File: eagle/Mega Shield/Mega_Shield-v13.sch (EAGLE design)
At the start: 27 parts, among them U1 LCD-16X2SILK, U2 LCD-16X2SILK, U3 MAX232PTH

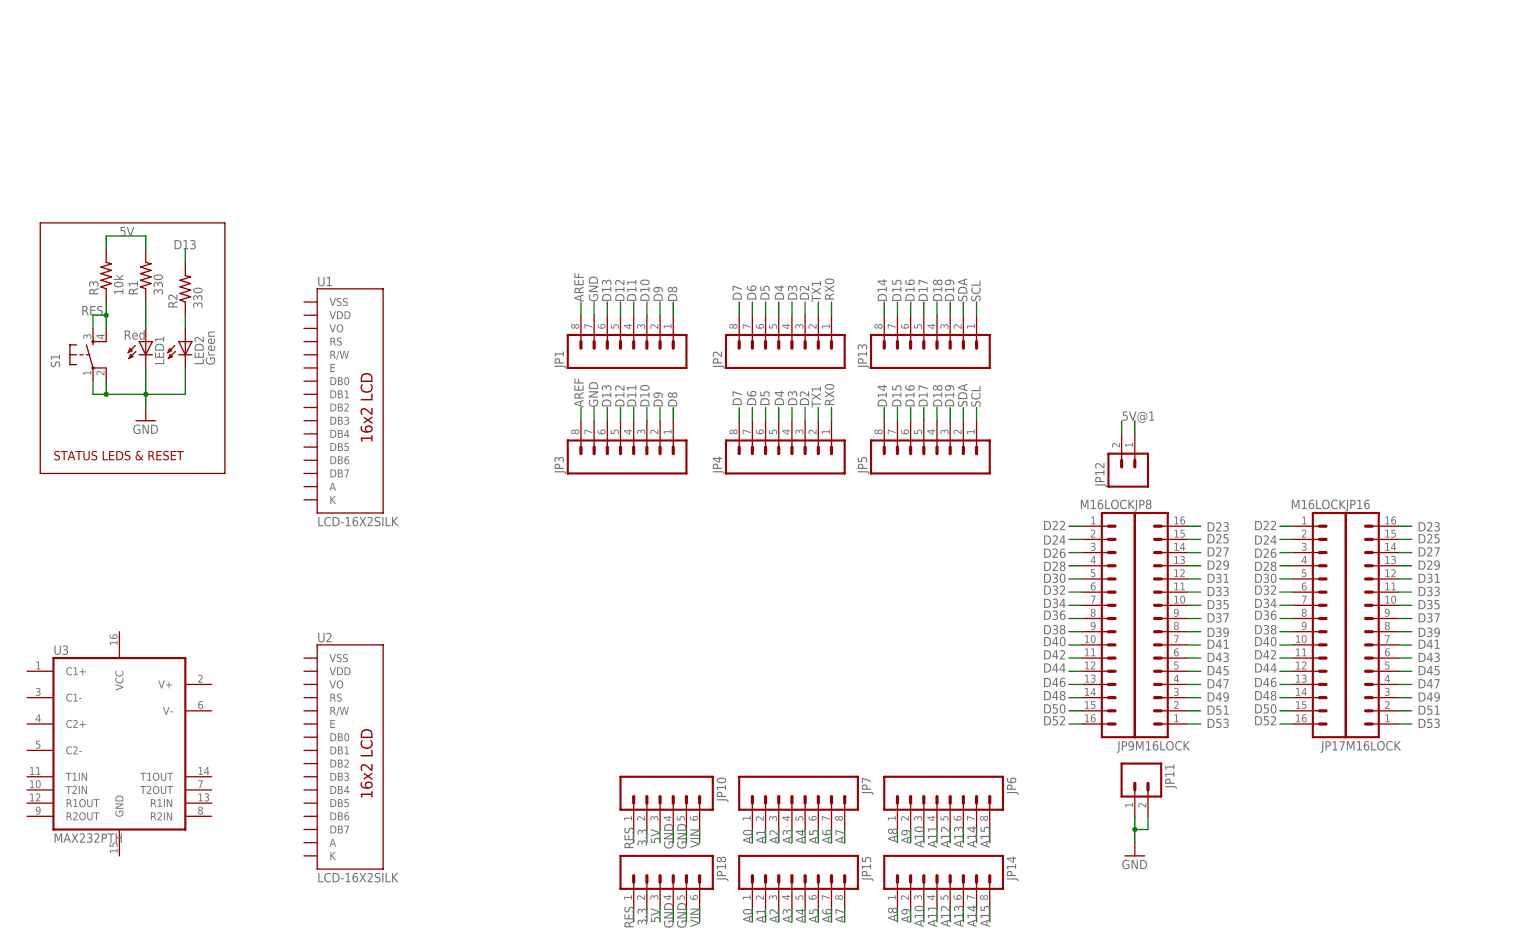
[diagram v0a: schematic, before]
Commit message: working on pcb, added main connector and lcds
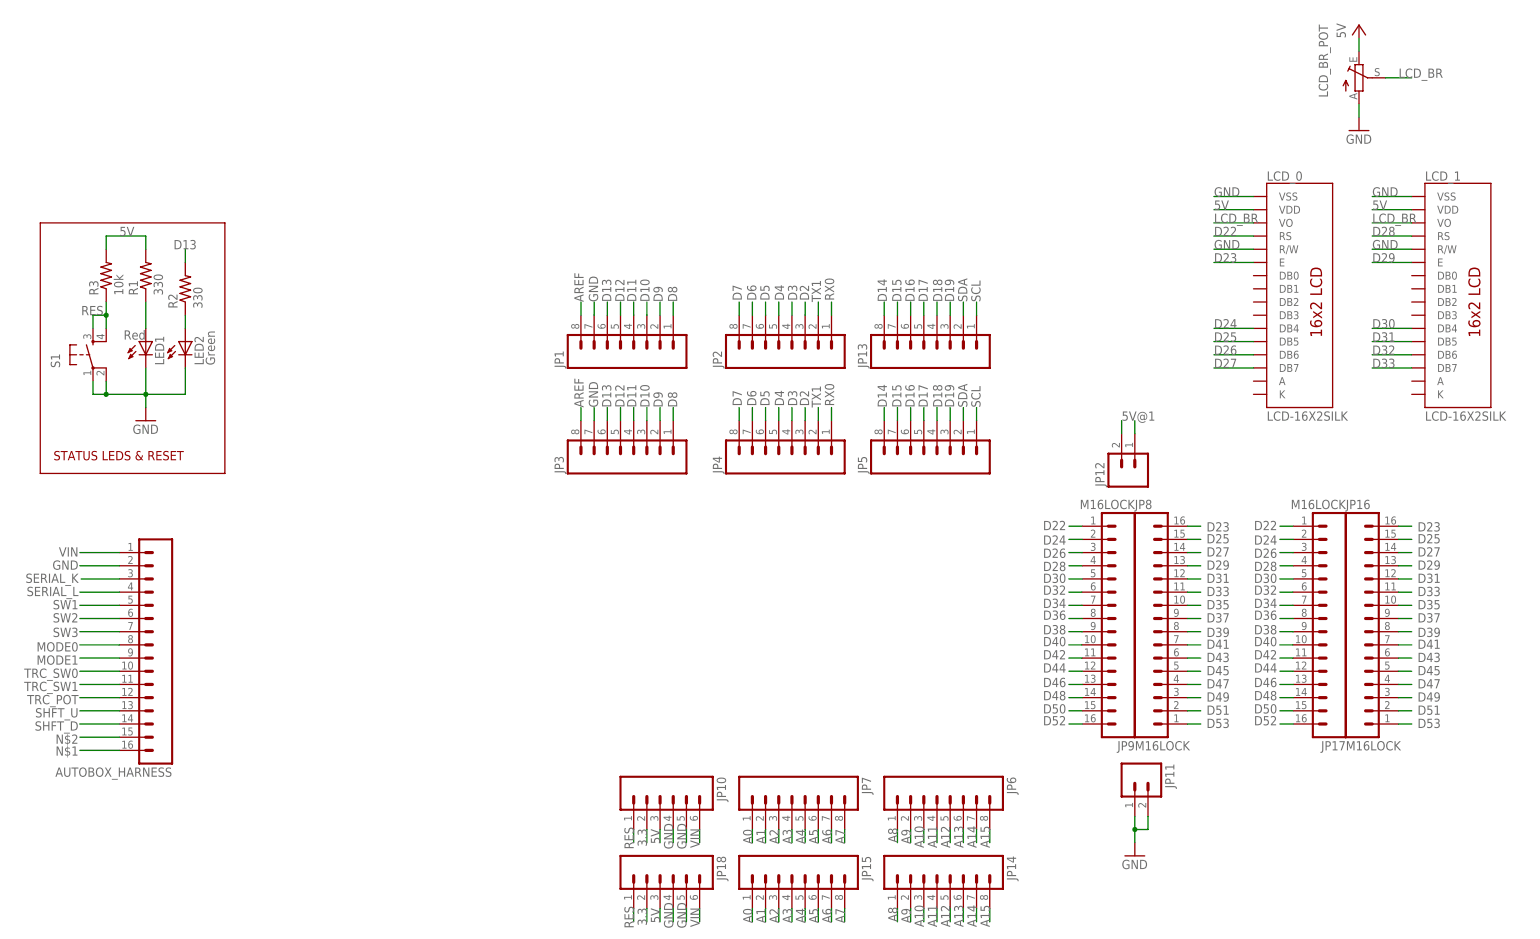
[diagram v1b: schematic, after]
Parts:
- removed U1, U2: LCD-16X2SILK, SparkFun-Displays:LCD-16X2SILK
- removed U3: MAX232PTH, SparkFun-DigitalIC:MAX232PTH
- added AUTOBOX_HARNESS: (no value), con-amp-quick:M16
- added LCD_0, LCD_1: LCD-16X2SILK, SparkFun-Displays:LCD-16X2SILK
- added LCD_BR_POT: (no value), pot:TRIM_EU-CA14V
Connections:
- new net LCD_BR: LCD_0.VO, LCD_1.VO, LCD_BR_POT.S
- new net MODE0: AUTOBOX_HARNESS.8
- new net MODE1: AUTOBOX_HARNESS.9
- new net N$1: AUTOBOX_HARNESS.16
- new net N$2: AUTOBOX_HARNESS.15
- new net SERIAL_K: AUTOBOX_HARNESS.3
- new net SERIAL_L: AUTOBOX_HARNESS.4
- new net SHFT_D: AUTOBOX_HARNESS.14
- new net SHFT_U: AUTOBOX_HARNESS.13
- new net SW1: AUTOBOX_HARNESS.5
- new net SW2: AUTOBOX_HARNESS.6
- new net SW3: AUTOBOX_HARNESS.7
- new net TRC_POT: AUTOBOX_HARNESS.12
- new net TRC_SW0: AUTOBOX_HARNESS.10
- new net TRC_SW1: AUTOBOX_HARNESS.11
- net 5V: now also LCD_0.VDD, LCD_1.VDD, LCD_BR_POT.E
- net D22: now also LCD_0.RS
- net D23: now also LCD_0.E
- net D24: now also LCD_0.DB4
- net D25: now also LCD_0.DB5
- net D26: now also LCD_0.DB6
- net D27: now also LCD_0.DB7
- net D28: now also LCD_1.RS
- net D29: now also LCD_1.E
- net D30: now also LCD_1.DB4
- net D31: now also LCD_1.DB5
- net D32: now also LCD_1.DB6
- net D33: now also LCD_1.DB7
- net GND: now also AUTOBOX_HARNESS.2, LCD_0.R/W, LCD_0.VSS, LCD_1.R/W, LCD_1.VSS, LCD_BR_POT.A
- net VIN: now also AUTOBOX_HARNESS.1

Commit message: more changes
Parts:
- added LED3: (no value), led:LED5MM
- added Q1, Q2, Q4: 2N3904, transistor-npn:2N3904
- added Q5: 2N3906, transistor-pnp:2N3906
- added R10, R4, R6, R8: 10k, SparkFun-Passives:RESISTOREZ
- added R5, R7, R9: 1k, SparkFun-Passives:RESISTOREZ
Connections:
- new net N$10: Q4.C, R10.1, R8.1
- new net N$3: Q1.C, R4.1
- new net N$4: Q1.B, R5.1
- new net N$5: Q5.C, R5.2, R7.2
- new net N$6: Q5.B, R6.1
- new net N$7: LED3.A, R7.1
- new net N$8: Q2.B, R10.2
- net 5V: now also JP12.2, R4.2, R8.2
- net 5V@1: no longer JP12.2
- net D18: now also Q4.B
- net D19: now also Q1.E
- net GND: now also LED3.C, Q2.E, Q4.E
- net SERIAL_K: now also Q2.C, R6.2, R9.1
- net VIN: now also Q5.E, R9.2
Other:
- note added: "K-LINE -> UART CONVERTER"
- note added: "RX1"
- note added: "TX1"
- moved on the sheet: AUTOBOX_HARNESS, LED1, LED2, R1, R2, R3, S1

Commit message: did a lot of pcb work
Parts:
- removed AUTOBOX_HARNESS: (no value), con-amp-quick:M16
- added ABOX_HARN, DSW_LG: (no value), Molex connectors:172064-0012
- added ABOX_PWR, DSW_SM, STEER: (no value), Molex connectors:172064-0004
- added CD4504BE: (no value), ic-package:DIL16S
- LCD_0, LCD_1: value LCD-16X2SILK -> 057-010-1; device SparkFun-Displays:LCD-16X2SILK -> con-panduit:057-010-1
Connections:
- removed net 5V@1: JP12.1
- removed net N$3: Q1.C, R4.1
- new net N$11: CD4504BE.2
- new net N$12: CD4504BE.3
- new net N$13: CD4504BE.4
- new net N$14: CD4504BE.5
- new net N$15: CD4504BE.6
- new net N$16: CD4504BE.7
- new net N$19: CD4504BE.15
- new net N$20: CD4504BE.14
- new net N$22: CD4504BE.12
- new net N$23: CD4504BE.11
- new net N$24: CD4504BE.10
- new net N$25: CD4504BE.9
- net 5V: now also CD4504BE.1, JP12.1, LCD_0-3.S, LCD_1-3.S; no longer LCD_0.VDD, LCD_1.VDD
- net D19: now also Q1.C, R4.1; no longer Q1.E
- net D22: now also LCD_0-7.S; no longer LCD_0.RS
- net D23: now also LCD_0-2.S; no longer LCD_0.E
- net D24: now also LCD_0-4.S; no longer LCD_0.DB4
- net D25: now also LCD_0-6.S; no longer LCD_0.DB5
- net D26: now also LCD_0-8.S; no longer LCD_0.DB6
- net D27: now also LCD_0-10.S; no longer LCD_0.DB7
- net D28: now also LCD_1-7.S; no longer LCD_1.RS
- net D29: now also LCD_1-2.S; no longer LCD_1.E
- net D30: now also LCD_1-4.S; no longer LCD_1.DB4
- net D31: now also LCD_1-6.S; no longer LCD_1.DB5
- net D32: now also LCD_1-8.S; no longer LCD_1.DB6
- net D33: now also LCD_1-10.S; no longer LCD_1.DB7
- net GND: now also ABOX_PWR.CKT2, CD4504BE.13, CD4504BE.8, LCD_0-1.S, LCD_0-9.S, LCD_1-1.S, LCD_1-9.S, Q1.E; no longer AUTOBOX_HARNESS.2, LCD_0.R/W, LCD_0.VSS, LCD_1.R/W, LCD_1.VSS
- net LCD_BR: now also LCD_0-5.S, LCD_1-5.S; no longer LCD_0.VO, LCD_1.VO
- net MODE0: now also ABOX_HARN.CKT6; no longer AUTOBOX_HARNESS.8
- net MODE1: now also ABOX_HARN.CKT7; no longer AUTOBOX_HARNESS.9
- net N$1: now also ABOX_HARN.CKT12; no longer AUTOBOX_HARNESS.16
- net N$2: now also ABOX_HARN.CKT11; no longer AUTOBOX_HARNESS.15
- net SERIAL_K: now also ABOX_HARN.CKT1; no longer AUTOBOX_HARNESS.3
- net SERIAL_L: now also ABOX_HARN.CKT2; no longer AUTOBOX_HARNESS.4
- net SHFT_D: now also ABOX_PWR.CKT4; no longer AUTOBOX_HARNESS.14
- net SHFT_U: now also ABOX_PWR.CKT3; no longer AUTOBOX_HARNESS.13
- net SW1: now also ABOX_HARN.CKT3; no longer AUTOBOX_HARNESS.5
- net SW2: now also ABOX_HARN.CKT4; no longer AUTOBOX_HARNESS.6
- net SW3: now also ABOX_HARN.CKT5; no longer AUTOBOX_HARNESS.7
- net TRC_POT: now also ABOX_HARN.CKT10; no longer AUTOBOX_HARNESS.12
- net TRC_SW0: now also ABOX_HARN.CKT8; no longer AUTOBOX_HARNESS.10
- net TRC_SW1: now also ABOX_HARN.CKT9; no longer AUTOBOX_HARNESS.11
- net VIN: now also ABOX_PWR.CKT1, CD4504BE.16; no longer AUTOBOX_HARNESS.1
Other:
- note added: "AI"
- note added: "AO"
- note added: "BI"
- note added: "BO"
- note added: "CI"
- note added: "CO"
- note added: "DI"
- note added: "DO"
- note added: "EI"
- note added: "EO"
- note added: "FI"
- note added: "FO"
- note added: "GND"
- note added: "LCD DISPLAYS"
- note added: "SEL"
- note added: "V_H"
- note added: "V_L"
- moved on the sheet: LCD_BR_POT, R4

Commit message: lots of board work
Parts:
- removed LCD_BR_POT: (no value), pot:TRIM_EU-CA14V
- added CD4504BE1: (no value), ic-package:DIL16S
- added R11: (no value), pot:TRIM_US-CT6
- added R12, R13, R14, R15, R16: 10k, SparkFun-Passives:RESISTOREZ
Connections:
- removed net N$1: ABOX_HARN.CKT12
- removed net N$11: CD4504BE.2
- removed net N$12: CD4504BE.3
- removed net N$13: CD4504BE.4
- removed net N$14: CD4504BE.5
- removed net N$15: CD4504BE.6
- removed net N$16: CD4504BE.7
- removed net N$2 (its old number): ABOX_HARN.CKT11
- removed net N$24: CD4504BE.10
- removed net N$25: CD4504BE.9
- removed net TRC_POT: ABOX_HARN.CKT10
- removed net TRC_SW0: ABOX_HARN.CKT8
- removed net TRC_SW1: ABOX_HARN.CKT9
- new net LAUNCHSW_12: CD4504BE.3, DSW_LG.CKT2, R13.2
- new net LAUNCHSW_LED: CD4504BE1.2, DSW_LG.CKT3
- new net LAUNCH_LED: ABOX_HARN.CKT11, CD4504BE1.3
- new net LAUNCH_SW: ABOX_HARN.CKT8, CD4504BE.2
- new net N$27: CD4504BE1.6
- new net N$28: CD4504BE1.7
- new net N$29: DSW_SM.CKT4
- new net N$32: CD4504BE1.15
- new net N$33: CD4504BE1.14
- new net N$35: CD4504BE1.12
- new net N$36: CD4504BE1.11
- new net N$37: CD4504BE1.10
- new net N$38: CD4504BE1.9
- new net N$97: DSW_SM.CKT3
- new net N$98: DSW_SM.CKT2
- new net N$99: DSW_SM.CKT1
- new net TRAC_LED: ABOX_HARN.CKT12, CD4504BE1.5
- new net TRA_CTL_LED: CD4504BE1.4, DSW_LG.CKT5
- new net TRA_CTL_POT: ABOX_HARN.CKT10, DSW_LG.CKT7
- new net TRA_CTL_SW: ABOX_HARN.CKT9, CD4504BE.4
- new net TRA_CTL_SW_12: CD4504BE.5, DSW_LG.CKT4, R14.2
- net 5V: now also CD4504BE.16, CD4504BE1.1, R11.E, R12.1; no longer CD4504BE.1, LCD_BR_POT.E
- net D22: now also CD4504BE.6; no longer LCD_0-7.S
- net D23: now also CD4504BE.10; no longer LCD_0-2.S
- net D24: now also DSW_LG.CKT6, R12.2; no longer LCD_0-4.S
- net D25: no longer LCD_0-6.S
- net D26: no longer LCD_0-8.S
- net D27: no longer LCD_0-10.S
- net D28: no longer LCD_1-7.S
- net D29: no longer LCD_1-2.S
- net D30: no longer LCD_1-4.S
- net D31: no longer LCD_1-6.S
- net D32: no longer LCD_1-8.S
- net D33: no longer LCD_1-10.S
- net D42: now also LCD_0-7.S
- net D43: now also LCD_0-2.S
- net D44: now also LCD_0-4.S
- net D45: now also LCD_0-6.S
- net D46: now also LCD_0-8.S
- net D47: now also LCD_0-10.S
- net D48: now also LCD_1-7.S
- net D49: now also LCD_1-2.S
- net D50: now also LCD_1-4.S
- net D51: now also LCD_1-6.S
- net D52: now also LCD_1-8.S
- net D53: now also LCD_1-10.S
- net GND: now also CD4504BE1.13, CD4504BE1.8, R11.A, R13.1, R14.1, R15.2, R16.1, STEER.CKT2; no longer LCD_BR_POT.A
- net LCD_BR: now also R11.S; no longer LCD_BR_POT.S
- net MODE0: now also DSW_LG.CKT8
- net MODE1: now also DSW_LG.CKT9
- net SHFT_D: now also CD4504BE.9, R16.2, STEER.CKT4
- net SHFT_U: now also CD4504BE.7, R15.1, STEER.CKT3
- net SW1: now also DSW_LG.CKT10
- net SW2: now also DSW_LG.CKT11
- net SW3: now also DSW_LG.CKT12
- net VIN: now also CD4504BE.1, CD4504BE1.16, DSW_LG.CKT1, STEER.CKT1; no longer CD4504BE.16
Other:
- note added: "GEAR RESET SW"
- note added: "HIGH TO LOW"
- note added: "LOW TO HIGH"
- note added: "VI"
- note added: "VO"
- note removed: "V_H"
- note removed: "V_L"
- moved on the sheet: DSW_SM, LCD_0-1, LCD_0-10, LCD_0-2, LCD_0-3, LCD_0-4, LCD_0-5, LCD_0-6, LCD_0-7, LCD_0-8, LCD_0-9, LCD_1-1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

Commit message: ordered pcbs
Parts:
- removed ABOX_HARN, DSW_LG: (no value), Molex connectors:172064-0012
- added ABOX_HARN_0, ABOX_HARN_1, ABOX_HARN_2, ABOX_HARN_3, DSW_LG_0, DSW_LG_1, DSW_LG_2: 5569, MHR14:5569
- added JP20, JP21, JP22, JP23, JP24, JP25, JP26, JP27: M12PTH, SparkFun-Connectors:M12PTH
- ABOX_PWR, DSW_SM, STEER: value (none) -> 5569; device Molex connectors:172064-0004 -> MHR14:5569
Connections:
- removed net N$98: DSW_SM.CKT2
- removed net N$99: DSW_SM.CKT1
- new net E_DSEN_LED: ABOX_HARN_3.CKT2, DSW_SM.CKT2
- new net E_DSEN_SW: ABOX_HARN_3.CKT3, STEER.CKT2
- new net GFD_LED: ABOX_HARN_3.CKT1, DSW_SM.CKT1
- net 5V: now also JP20.12, JP21.12, JP22.12, JP23.12, JP24.12, JP25.12, JP26.12, JP27.12
- net A7: now also ABOX_HARN_3.CKT4
- net D24: now also DSW_LG_1.CKT2; no longer DSW_LG.CKT6
- net GND: now also JP20.1, JP21.1, JP22.1, JP23.1, JP24.1, JP25.1, JP26.1, JP27.1; no longer STEER.CKT2
- net LAUNCHSW_12: now also DSW_LG_0.CKT2; no longer DSW_LG.CKT2
- net LAUNCHSW_LED: now also DSW_LG_0.CKT3; no longer DSW_LG.CKT3
- net LAUNCH_LED: now also ABOX_HARN_2.CKT3; no longer ABOX_HARN.CKT11
- net LAUNCH_SW: now also ABOX_HARN_1.CKT4; no longer ABOX_HARN.CKT8
- net MODE0: now also ABOX_HARN_1.CKT2, DSW_LG_1.CKT4; no longer ABOX_HARN.CKT6, DSW_LG.CKT8
- net MODE1: now also ABOX_HARN_1.CKT3, DSW_LG_2.CKT1; no longer ABOX_HARN.CKT7, DSW_LG.CKT9
- net SERIAL_K: now also ABOX_HARN_0.CKT1; no longer ABOX_HARN.CKT1
- net SERIAL_L: now also ABOX_HARN_0.CKT2; no longer ABOX_HARN.CKT2
- net SW1: now also ABOX_HARN_0.CKT3, DSW_LG_2.CKT2; no longer ABOX_HARN.CKT3, DSW_LG.CKT10
- net SW2: now also ABOX_HARN_0.CKT4, DSW_LG_2.CKT3; no longer ABOX_HARN.CKT4, DSW_LG.CKT11
- net SW3: now also ABOX_HARN_1.CKT1, DSW_LG_2.CKT4; no longer ABOX_HARN.CKT5, DSW_LG.CKT12
- net TRAC_LED: now also ABOX_HARN_2.CKT4; no longer ABOX_HARN.CKT12
- net TRA_CTL_LED: now also DSW_LG_1.CKT1; no longer DSW_LG.CKT5
- net TRA_CTL_POT: now also ABOX_HARN_2.CKT2, DSW_LG_1.CKT3; no longer ABOX_HARN.CKT10, DSW_LG.CKT7
- net TRA_CTL_SW: now also ABOX_HARN_2.CKT1; no longer ABOX_HARN.CKT9
- net TRA_CTL_SW_12: now also DSW_LG_0.CKT4; no longer DSW_LG.CKT4
- net VIN: now also DSW_LG_0.CKT1; no longer DSW_LG.CKT1
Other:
- note added: "FUELG"
- note added: "INLINE RESISTORS"
- moved on the sheet: ABOX_PWR, DSW_SM, R12, STEER
